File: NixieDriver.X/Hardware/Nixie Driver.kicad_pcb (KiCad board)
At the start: 2 copper layers, 21.1 x 31.8 mm, 18 parts, among them J1 Conn_02x03_Odd_Even, J2 Conn_02x03_Odd_Even, Q0 MMBTA42LT1G, Q1 MMBTA42LT1G, Q10 MMBTA42LT1G, Q2 MMBTA42LT1G, Q3 MMBTA42LT1G, Q4 MMBTA42LT1G, Q5 MMBTA42LT1G, Q6 MMBTA42LT1G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

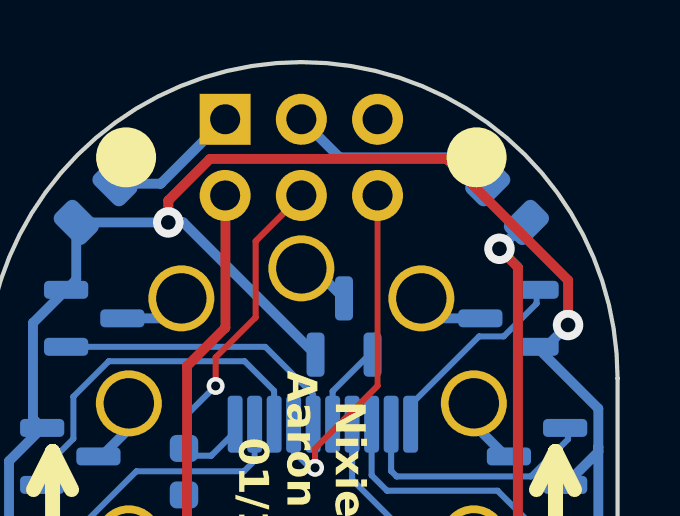
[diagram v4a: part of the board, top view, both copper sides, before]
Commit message: Upsized current-limiting resistor
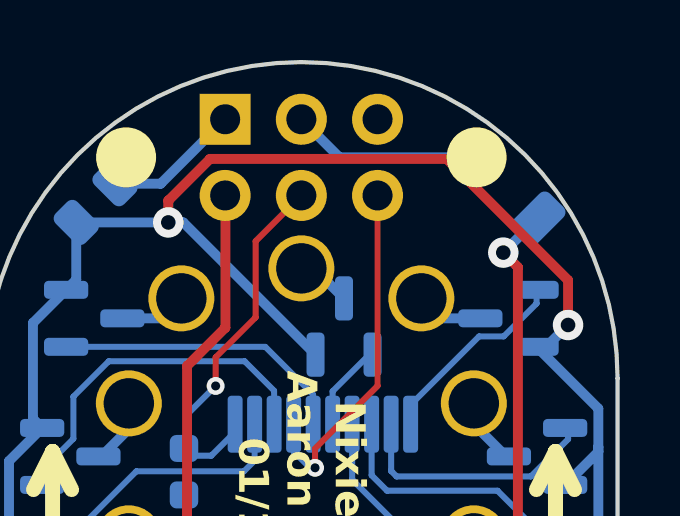
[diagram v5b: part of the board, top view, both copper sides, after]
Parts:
- R1: footprint Resistor_SMD:R_0805_2012Metric -> Resistor_SMD:R_1206_3216Metric
- moved R1 0.51 mm to (159.3, 89.9)
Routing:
- net Vnn: track 7.10 -> 6.36 mm
- net Net-(V1-V+): track 20.7 -> 21.3 mm
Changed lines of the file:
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@@
 		)
 	)
-	(footprint "Resistor_SMD:R_0805_2012Metric"
-		(layer "B.Cu")
-		(at 159.258 90.424 135)
-		(descr "Resistor SMD 0805 (2012 Metric), square (rectangular) end terminal, IPC_7351 nominal, (Body size source: IPC-SM-782 page 72, https://www.pcb-3d.com/wordpress/wp-content/uploads/ipc-sm-782a_amendment_1_and_2.pdf), generated with kicad-footprint-generator")
+	(footprint "Resistor_SMD:R_1206_3216Metric"
+		(layer "B.Cu")
+		(at 159.258 89.916 135)
+		(descr "Resistor SMD 1206 (3216 Metric), square (rectangular) end terminal, IPC_7351 nominal, (Body size source: IPC-SM-782 page 72, https://www.pcb-3d.com/wordpress/wp-content/uploads/ipc-sm-782a_amendment_1_and_2.pdf), generated with kicad-footprint-generator")
 		(tags "resistor")
 		(property "Reference" "R1"
-			(at 0 -1.796051 135)
+			(at 0 -1.796051 -45)
 			(layer "B.SilkS")
 			(effects
@@
 		)
 		(property "Value" "20k"
-			(at 0 -1.65 135)
+			(at 0 -1.82 -45)
 			(layer "B.Fab")
 			(effects
@@
 			)
 		)
-		(property "Footprint" "Resistor_SMD:R_0805_2012Metric"
+		(property "Footprint" "Resistor_SMD:R_1206_3216Metric"
 			(at 0 0 -45)
 			(unlocked yes)
@@
 		(attr smd)
 		(fp_line
-			(start 0.227064 -0.735)
-			(end -0.227064 -0.735)
+			(start 0.727064 -0.91)
+			(end -0.727064 -0.91)
 			(stroke
 				(width 0.12)
@@
 		)
 		(fp_line
-			(start 0.227064 0.735)
-			(end -0.227064 0.735)
+			(start 0.727064 0.91)
+			(end -0.727064 0.91)
 			(stroke
 				(width 0.12)
@@
 		)
 		(fp_line
-			(start 1.68 -0.95)
-			(end 1.68 0.95)
+			(start 2.28 -1.12)
+			(end 2.28 1.12)
 			(stroke
 				(width 0.05)
@@
 		)
 		(fp_line
-			(start 1.68 0.95)
-			(end -1.68 0.95)
+			(start 2.28 1.12)
+			(end -2.28 1.12)
 			(stroke
 				(width 0.05)
@@
 		)
 		(fp_line
-			(start -1.68 -0.95)
-			(end 1.68 -0.95)
+			(start -2.28 -1.12)
+			(end 2.28 -1.12)
 			(stroke
 				(width 0.05)
@@
 		)
 		(fp_line
-			(start -1.68 0.95)
-			(end -1.68 -0.95)
+			(start -2.28 1.12)
+			(end -2.28 -1.12)
 			(stroke
 				(width 0.05)
@@
 		)
 		(fp_line
-			(start 1 -0.625)
-			(end 1 0.625)
+			(start 1.6 -0.8)
+			(end 1.6 0.8)
 			(stroke
 				(width 0.1)
@@
 		)
 		(fp_line
-			(start 1 0.625)
-			(end -1 0.625)
+			(start 1.6 0.8)
+			(end -1.6 0.8)
 			(stroke
 				(width 0.1)
@@
 		)
 		(fp_line
-			(start -1 -0.625)
-			(end 1 -0.625)
+			(start -1.6 -0.8)
+			(end 1.6 -0.8)
 			(stroke
 				(width 0.1)
@@
 		)
 		(fp_line
-			(start -1 0.625)
-			(end -1 -0.625)
+			(start -1.6 0.8)
+			(end -1.6 -0.8)
 			(stroke
 				(width 0.1)
@@
 		)
 		(fp_text user "${REFERENCE}"
-			(at 0 0 135)
+			(at 0 0 -45)
 			(layer "B.Fab")
 			(effects
 				(font
-					(size 0.5 0.5)
-					(thickness 0.08)
+					(size 0.8 0.8)
+					(thickness 0.12)
 				)
 				(justify mirror)
@@
 		)
 		(pad "1" smd roundrect
-			(at -0.9125 0 135)
-			(size 1.025 1.4)
+			(at -1.4625 0 135)
+			(size 1.125 1.75)
 			(layers "B.Cu" "B.Paste" "B.Mask")
-			(roundrect_rratio 0.243902)
+			(roundrect_rratio 0.222222)
 			(net 31 "Net-(V1-V+)")
 			(pintype "passive")
 		)
 		(pad "2" smd roundrect
-			(at 0.9125 0 135)
-			(size 1.025 1.4)
+			(at 1.4625 0 135)
+			(size 1.125 1.75)
 			(layers "B.Cu" "B.Paste" "B.Mask")
-			(roundrect_rratio 0.243902)
+			(roundrect_rratio 0.222222)
 			(net 29 "Vnn")
 			(pintype "passive")
 		)
-		(model "${KICAD8_3DMODEL_DIR}/Resistor_SMD.3dshapes/R_0805_2012Metric.wrl"
+		(model "${KICAD8_3DMODEL_DIR}/Resistor_SMD.3dshapes/R_1206_3216Metric.wrl"
 			(offset
 				(xyz 0 0 0)
@@
 	)
 	(segment
+		(start 158.205712 88.9)
+		(end 158.223856 88.881856)
+		(width 0.33)
+		(layer "B.Cu")
+		(net 29)
+	)
+	(segment
 		(start 153.67 88.9)
-		(end 157.734 88.9)
-		(width 0.33)
-		(layer "B.Cu")
-		(net 29)
-	)
-	(segment
-		(start 157.734 88.9)
-		(end 158.612765 89.778765)
+		(end 158.205712 88.9)
 		(width 0.33)
 		(layer "B.Cu")
@@
 	)
 	(segment
-		(start 159.004 91.948)
+		(start 159.131 92.075)
 		(end 159.6182 92.5622)
+		(width 0.33)
+		(layer "F.Cu")
+		(net 31)
+	)
+	(segment
+		(start 159.6182 92.5622)
+		(end 159.6182 106.708149)
+		(width 0.33)
+		(layer "F.Cu")
+		(net 31)
+	)
+	(segment
+		(start 156.726349 109.6)
+		(end 156.4 109.6)
 		(width 0.33)
 		(layer "F.Cu")
@@
 		(net 31)
 	)
-	(segment
-		(start 156.726349 109.6)
-		(end 156.4 109.6)
-		(width 0.33)
-		(layer "F.Cu")
-		(net 31)
-	)
-	(segment
-		(start 159.6182 92.5622)
-		(end 159.6182 106.708149)
-		(width 0.33)
-		(layer "F.Cu")
-		(net 31)
-	)
 	(via
-		(at 159.004 91.948)
+		(at 159.131 92.075)
 		(size 1.016)
 		(drill 0.485667)
@@
 	)
 	(segment
-		(start 159.882765 91.069235)
+		(start 160.173053 91.069235)
 		(end 159.903235 91.069235)
 		(width 0.33)
@@
 	)
 	(segment
-		(start 159.004 91.948)
-		(end 159.882765 91.069235)
-		(width 0.33)
-		(layer "B.Cu")
+		(start 160.292144 90.950144)
+		(end 160.173053 91.069235)
+		(width 0.33)
+		(layer "B.Cu")
+		(net 31)
+	)
+	(segment
+		(start 160.255856 90.950144)
+		(end 160.292144 90.950144)
+		(width 0.33)
+		(layer "B.Cu")
+		(net 31)
+	)
+	(segment
+		(start 159.131 92.075)
+		(end 160.255856 90.950144)
+		(width 0.33)
+		(layer "B.Cu")
